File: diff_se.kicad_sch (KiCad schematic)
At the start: 7 parts

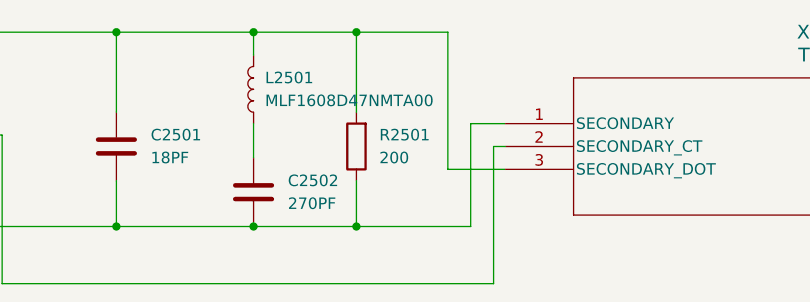
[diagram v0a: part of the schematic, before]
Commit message: Schematic Changes
Added Manufacturer/MPN/Description Fields to parts
Added libraries to project
Modified FMC schematic to use new symbol
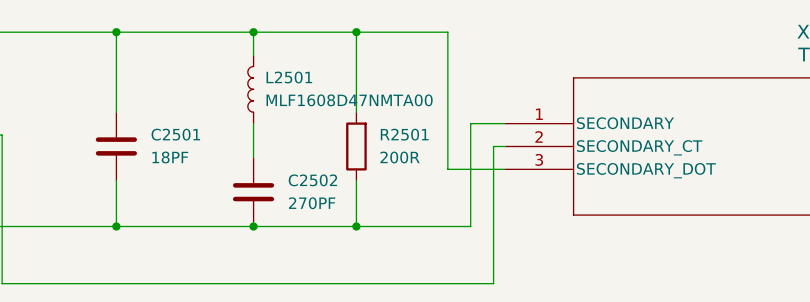
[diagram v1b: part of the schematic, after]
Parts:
- C2501: Manufacturer (none) -> Samsung; Manufacturer Part Number (none) -> CL10C180JB8NNNC
- C2502: Manufacturer (none) -> Murata; Manufacturer Part Number (none) -> GRM1885C1H271JA01D
- C2503, C2504: Manufacturer (none) -> Murata; Manufacturer Part Number (none) -> GRM1885C1H102JA01D
- L2501: Manufacturer (none) -> TDK; Manufacturer Part Number (none) -> MLF1608D47NMTA00
- R2501: value 200 -> 200R; Manufacturer (none) -> Susumu; Manufacturer Part Number (none) -> RR0816P-201-D
- XMER2501: Manufacturer (none) -> Mini-Circuits; Manufacturer Part Number (none) -> TCM4-19+
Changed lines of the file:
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@@
 			)
 		)
-		(property "Value" "200"
+		(property "Value" "200R"
 			(at 104.14 87.6299 0)
 			(effects
@@
 			)
 		)
-		(property "Description" "Resistor"
+		(property "Description" "RES SMD 200 OHM 0.5% 1/16W 0603"
 			(at 101.6 86.36 0)
 			(effects
@@
 		(property "Vendor" "digikey:RR08P200DCT-ND"
 			(at 203.2 0 0)
+			(effects
+				(font
+					(size 1.27 1.27)
+				)
+				(hide yes)
+			)
+		)
+		(property "Manufacturer" "Susumu "
+			(at 101.6 86.36 0)
+			(effects
+				(font
+					(size 1.27 1.27)
+				)
+				(hide yes)
+			)
+		)
+		(property "Manufacturer Part Number" "RR0816P-201-D "
+			(at 101.6 86.36 0)
 			(effects
 				(font
@@
 			)
 		)
-		(property "Description" "Unpolarized capacitor"
+		(property "Description" "CAP CER 1000PF 50V C0G/NP0 0603"
 			(at 204.47 88.9 0)
 			(effects
@@
 		(property "Vendor" "digikey:490-1451-1-ND"
 			(at 115.57 293.37 0)
+			(effects
+				(font
+					(size 1.27 1.27)
+				)
+				(hide yes)
+			)
+		)
+		(property "Manufacturer" "Murata"
+			(at 204.47 88.9 0)
+			(effects
+				(font
+					(size 1.27 1.27)
+				)
+				(hide yes)
+			)
+		)
+		(property "Manufacturer Part Number" "GRM1885C1H102JA01D "
+			(at 204.47 88.9 0)
 			(effects
 				(font
@@
 			)
 		)
-		(property "Description" "Inductor"
+		(property "Description" "FIXED IND 47NH 200MA 200MOHM SMD"
 			(at 90.17 80.01 0)
 			(effects
@@
 		(property "Vendor" "digikey:445-1000-1-ND"
 			(at 180.34 0 0)
+			(effects
+				(font
+					(size 1.27 1.27)
+				)
+				(hide yes)
+			)
+		)
+		(property "Manufacturer" "TDK"
+			(at 90.17 80.01 0)
+			(effects
+				(font
+					(size 1.27 1.27)
+				)
+				(hide yes)
+			)
+		)
+		(property "Manufacturer Part Number" "MLF1608D47NMTA00 "
+			(at 90.17 80.01 0)
 			(effects
 				(font
@@
 			)
 		)
-		(property "Description" "Unpolarized capacitor"
+		(property "Description" "CAP CER 1000PF 50V C0G/NP0 0603"
 			(at 204.47 83.82 0)
 			(effects
@@
 		(property "Vendor" "digikey:490-1451-1-ND"
 			(at 120.65 -120.65 0)
+			(effects
+				(font
+					(size 1.27 1.27)
+				)
+				(hide yes)
+			)
+		)
+		(property "Manufacturer" "Murata"
+			(at 204.47 83.82 0)
+			(effects
+				(font
+					(size 1.27 1.27)
+				)
+				(hide yes)
+			)
+		)
+		(property "Manufacturer Part Number" "GRM1885C1H102JA01D "
+			(at 204.47 83.82 0)
 			(effects
 				(font
@@
 			)
 		)
-		(property "Description" "Unpolarized capacitor"
+		(property "Description" "CAP CER 270PF 50V C0G/NP0 0603"
 			(at 90.17 91.44 0)
 			(effects
@@
 		(property "Vendor" "digikey:490-1437-1-ND"
 			(at 180.34 0 0)
+			(effects
+				(font
+					(size 1.27 1.27)
+				)
+				(hide yes)
+			)
+		)
+		(property "Manufacturer" "Murata"
+			(at 90.17 91.44 0)
+			(effects
+				(font
+					(size 1.27 1.27)
+				)
+				(hide yes)
+			)
+		)
+		(property "Manufacturer Part Number" "GRM1885C1H271JA01D"
+			(at 90.17 91.44 0)
 			(effects
 				(font
@@
 			)
 		)
-		(property "Description" "Unpolarized capacitor"
+		(property "Description" "CAP CER 18PF 50V C0G/NP0 0603"
 			(at 74.93 86.36 0)
 			(effects
@@
 		(property "Vendor" "digikey:1276-1089-1-ND"
 			(at 149.86 0 0)
+			(effects
+				(font
+					(size 1.27 1.27)
+				)
+				(hide yes)
+			)
+		)
+		(property "Manufacturer" "Samsung"
+			(at 74.93 86.36 0)
+			(effects
+				(font
+					(size 1.27 1.27)
+				)
+				(hide yes)
+			)
+		)
+		(property "Manufacturer Part Number" "CL10C180JB8NNNC"
+			(at 74.93 86.36 0)
 			(effects
 				(font
@@
 			)
 		)
-		(property "Description" ""
+		(property "Description" "1:4 CORE & WIRE TRANSFORMER, 10"
 			(at 118.11 83.82 0)
 			(effects
@@
 			(effects
 				(font
+					(size 1.27 1.27)
+				)
+				(hide yes)
+			)
+		)
+		(property "Manufacturer" "Mini-Circuits "
+			(at 118.11 83.82 0)
+			(effects
+				(font
+					(size 1.27 1.27)
+				)
+				(hide yes)
+			)
+		)
+		(property "Manufacturer Part Number" "TCM4-19+ "
+			(at 118.11 83.82 0)
+			(effects
+				(font

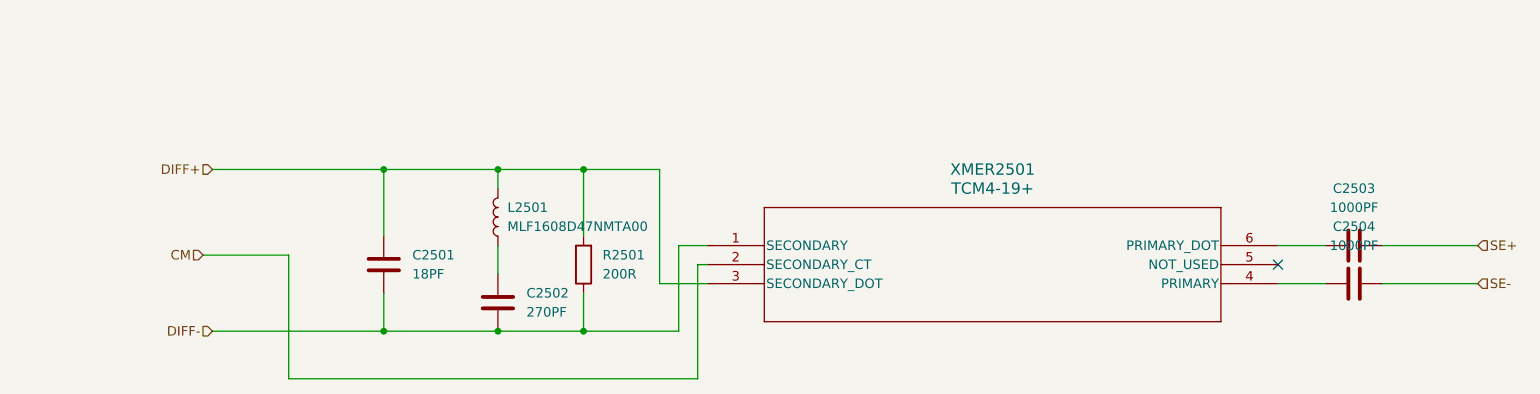
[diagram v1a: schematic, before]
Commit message: Schematics update
Cleaned up RF ADC and front end sections.
Verified that changes did not changes anything about the layout.
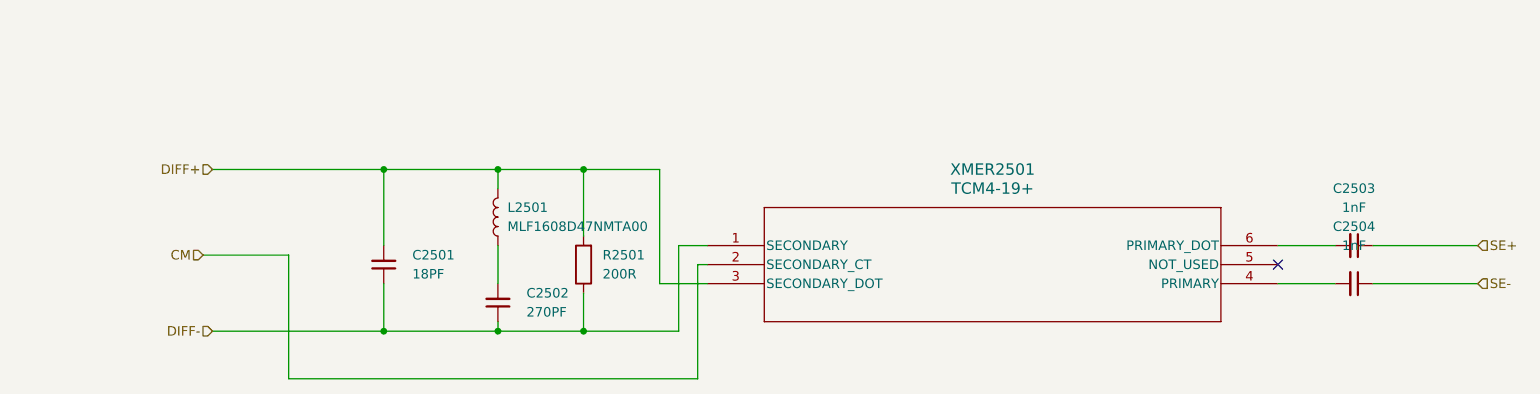
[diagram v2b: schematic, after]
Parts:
- C2501, C2502: symbol Device:C -> Device:C_Small
- C2503, C2504: value 1000PF -> 1nF; symbol Device:C -> Device:C_Small
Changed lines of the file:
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@@
 	(paper "A4")
+	(junction
+		(at 90.17 95.25)
+		(diameter 0)
+		(color 0 0 0 0)
+	)
 	(junction
 		(at 101.6 73.66)
@@
 	)
 	(junction
-		(at 90.17 95.25)
-		(diameter 0)
-		(color 0 0 0 0)
-	)
-	(junction
 		(at 74.93 95.25)
 		(diameter 0)
@@
 	(wire
 		(pts
-			(xy 74.93 73.66) (xy 74.93 82.55)
+			(xy 74.93 73.66) (xy 74.93 83.82)
 		)
 		(stroke
@@
 	(wire
 		(pts
-			(xy 74.93 90.17) (xy 74.93 95.25)
-		)
-		(stroke
-			(width 0)
-			(type default)
-		)
-	)
-	(wire
-		(pts
-			(xy 90.17 83.82) (xy 90.17 87.63)
+			(xy 74.93 88.9) (xy 74.93 95.25)
+		)
+		(stroke
+			(width 0)
+			(type default)
+		)
+	)
+	(wire
+		(pts
+			(xy 90.17 83.82) (xy 90.17 88.9)
 		)
 		(stroke
@@
 	(wire
 		(pts
-			(xy 208.28 83.82) (xy 220.98 83.82)
-		)
-		(stroke
-			(width 0)
-			(type default)
-		)
-	)
-	(wire
-		(pts
-			(xy 194.31 83.82) (xy 200.66 83.82)
+			(xy 207.01 83.82) (xy 220.98 83.82)
+		)
+		(stroke
+			(width 0)
+			(type default)
+		)
+	)
+	(wire
+		(pts
+			(xy 194.31 83.82) (xy 201.93 83.82)
+		)
+		(stroke
+			(width 0)
+			(type default)
+		)
+	)
+	(wire
+		(pts
+			(xy 90.17 93.98) (xy 90.17 95.25)
 		)
 		(stroke
@@
 	(wire
 		(pts
-			(xy 208.28 88.9) (xy 220.98 88.9)
-		)
-		(stroke
-			(width 0)
-			(type default)
-		)
-	)
-	(wire
-		(pts
-			(xy 194.31 88.9) (xy 200.66 88.9)
+			(xy 207.01 88.9) (xy 220.98 88.9)
+		)
+		(stroke
+			(width 0)
+			(type default)
+		)
+	)
+	(wire
+		(pts
+			(xy 194.31 88.9) (xy 201.93 88.9)
 		)
 		(stroke
@@
 	)
 	(symbol
-		(lib_id "Device:C")
+		(lib_id "Device:C_Small")
 		(at 204.47 88.9 270)
 		(mirror x)
@@
 			)
 		)
-		(property "Value" "1000PF"
+		(property "Value" "1nF"
 			(at 204.47 83.82 90)
 			(effects
@@
 	)
 	(symbol
-		(lib_id "Device:C")
+		(lib_id "Device:C_Small")
 		(at 204.47 83.82 270)
 		(unit 1)
@@
 			)
 		)
-		(property "Value" "1000PF"
+		(property "Value" "1nF"
 			(at 204.47 78.74 90)
 			(effects
@@
 	)
 	(symbol
-		(lib_id "Device:C")
+		(lib_id "Device:C_Small")
 		(at 90.17 91.44 180)
 		(unit 1)
@@
 	)
 	(symbol
-		(lib_id "Device:C")
+		(lib_id "Device:C_Small")
 		(at 74.93 86.36 180)
 		(unit 1)

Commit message: Updated some Schematics
- updated slowmon schematic
- updated diff to se schematic
- cleaned up DRC/ERC errors
No changes were made that effected the PCB layout
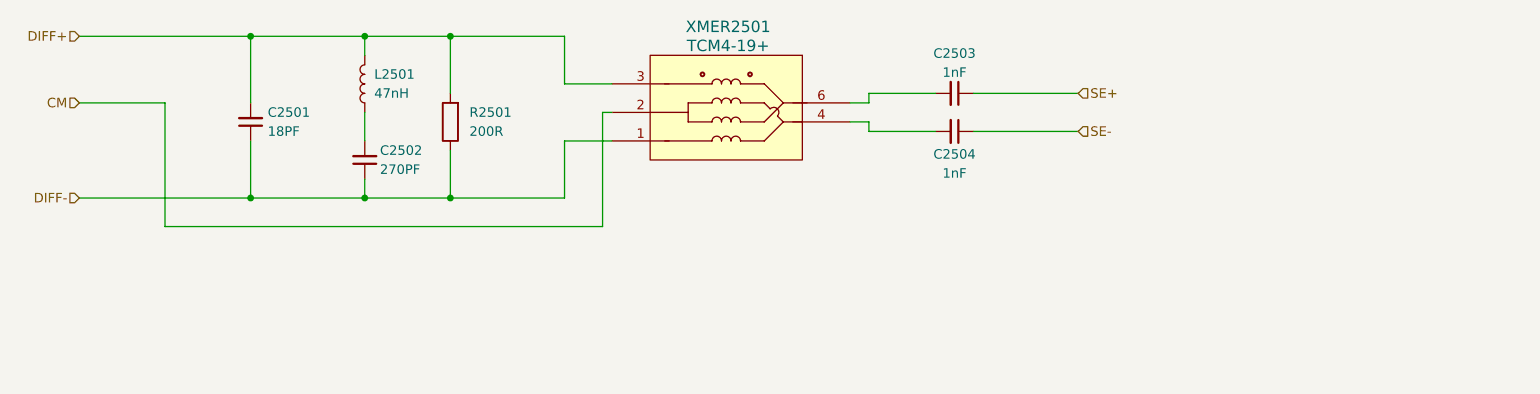
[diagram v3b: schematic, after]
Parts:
- L2501: value MLF1608D47NMTA00 -> 47nH
- XMER2501: symbol 001_symbol:TCM4-19+ -> Zest_Custom:TCM4-19+
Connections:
- no-connect marks 1 -> 0
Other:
- moved on the sheet: C2501, C2502, C2503, C2504, L2501, R2501

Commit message: Made MPEX Changes
- Minimal Changes from main branch
- Changed ADC input section TCM4-19+ to TC1-1+
- Changed DAC output section TCM4-19+ to TC4-6T+
- Changed Silkscreen text to read MPEX Zest
- Added Documentation folder with pdfs of schematics and pcb prints
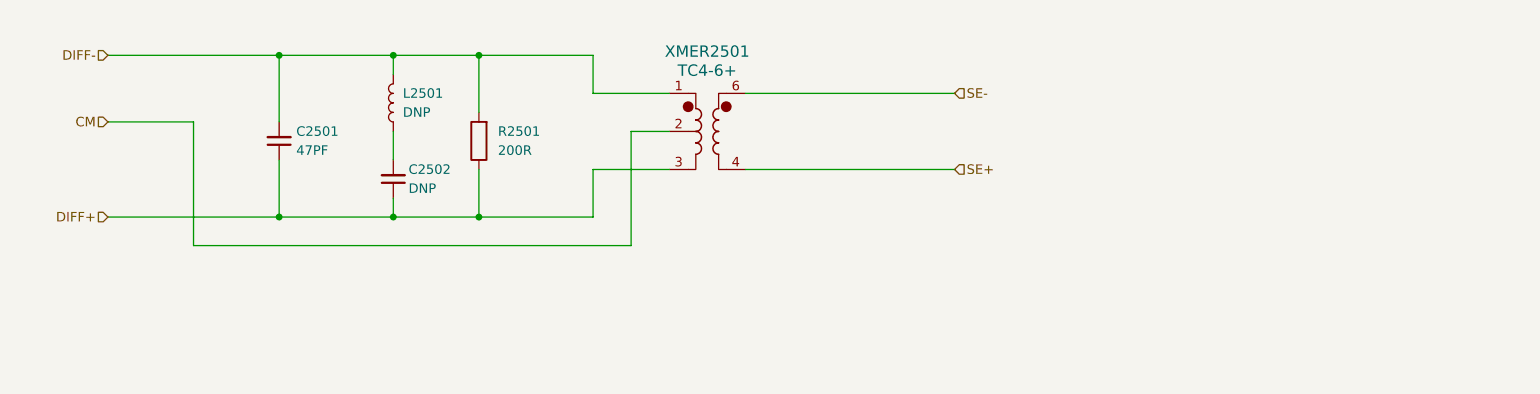
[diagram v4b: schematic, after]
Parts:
- removed C2503, C2504: 1nF, Capacitor_SMD:C_0603_1608Metric, symbol Device:C_Small
- C2501: value 18PF -> 47PF
- C2502: value 270PF -> DNP
- L2501: value 47nH -> DNP
- XMER2501: value TCM4-19+ -> TC4-6+; footprint 001_download:DB714_MNC -> Transformer_SMD:Transformer_MiniCircuits_AT224-1A; symbol Zest_Custom:TCM4-19+ -> Zest_Custom:TC4-6; Manufacturer Part Number TCM4-19+ -> TC4-6+; Vendor digikey:TCM4-19+ -> digikey:3157-TC4-6T+CT-ND
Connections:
- net DIFF+: now also C2501.1, C2502.1, R2501.1; no longer C2501.2, L2501.2, R2501.2
- net DIFF-: now also C2501.2, L2501.2, R2501.2; no longer C2501.1, C2502.1, R2501.1
- net SE+: now also XMER2501.4
- net SE-: now also XMER2501.6
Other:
- moved on the sheet: C2501, C2502, L2501, R2501

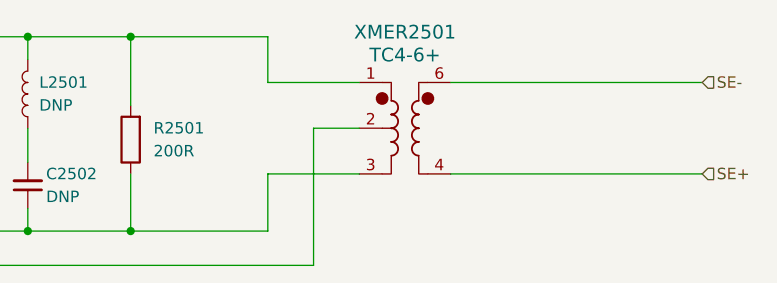
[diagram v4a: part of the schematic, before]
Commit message: Further Project cleanup
-Added BOM and fabrication files
-updated all documentation files
- Added suggested DC blocking cap at DAC outputs

-Set DRC to 5mil trace and space and fixed various violations detailed below
- Removed various small tracks overlapping IC pads on U2701,U2901,U3101,U3201
- Spaced vias 5 mil apart around U701, U201, 1201
- Moved LMK_CLKout3 pair on In4 layer away from PMOD1_1 pin
- adjusted track into pin47 on U701 to clear pin 48
- adjusted trace under U903 to give more room from ground pads/vias
- spaced out vias around pins45/46 of U201

-Many tweak to trace to go through the center of pad throughout the design
-An example is the trace around C3005
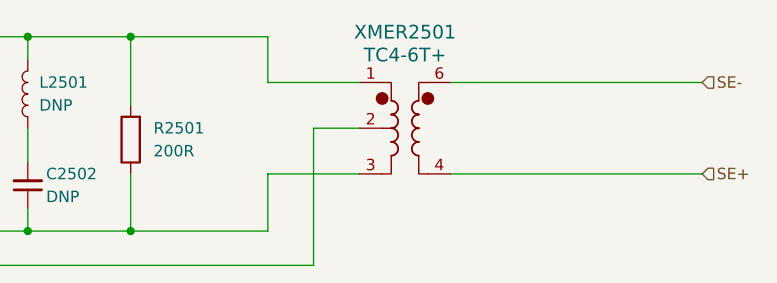
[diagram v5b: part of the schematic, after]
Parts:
- C2501: Manufacturer Samsung -> KYOCERA AVX; Manufacturer Part Number CL10C180JB8NNNC -> KGM15ACG1H470FT; Vendor digikey:1276-1089-1-ND -> digikey:478-KGM15ACG1H470FTCT-ND
- XMER2501: value TC4-6+ -> TC4-6T+
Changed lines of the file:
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@@
 			)
 		)
-		(property "Description" "CAP CER 18PF 50V C0G/NP0 0603"
+		(property "Description" "CAP CER 47PF 50V C0G/NP0 0603"
 			(at 60.96 69.85 0)
 			(effects
@@
 			)
 		)
-		(property "Vendor" "digikey:1276-1089-1-ND"
+		(property "Vendor" "digikey:478-KGM15ACG1H470FTCT-ND"
 			(at 135.89 -16.51 0)
 			(effects
@@
 			)
 		)
-		(property "Manufacturer" "Samsung"
+		(property "Manufacturer" "KYOCERA AVX"
 			(at 60.96 69.85 0)
 			(effects
@@
 			)
 		)
-		(property "Manufacturer Part Number" "CL10C180JB8NNNC"
+		(property "Manufacturer Part Number" "KGM15ACG1H470FT"
 			(at 60.96 69.85 0)
 			(effects
@@
 			)
 		)
-		(property "Value" "TC4-6+"
+		(property "Value" "TC4-6T+"
 			(at 118.11 60.452 0)
 			(effects
@@
 			)
 		)
-		(property "Datasheet" "TC4-6+"
+		(property "Datasheet" "TC4-6T+"
 			(at 123.19 60.96 0)
 			(effects

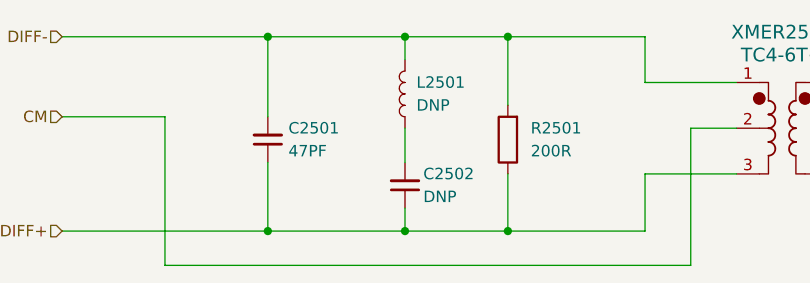
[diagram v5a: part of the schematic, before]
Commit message: Properly attributed DNP parts; Added Fabrication Notes
-Properly attributed various DNP in the project;
This includes: C210.C710,C1601,C2502,C2602,L2501,R1507,L2601,R1601,R805
- I changed the accelerometer and microphone (+it's filter)to DNP parts
  Note: both of these are obsolete parts. As part of this change I Changed R1602 (part of mic buffer) from 220k to 0R. The removal of these parts should in no way negatively effect the rest of the circuit.
-I fixed the 'value' attribute of XMER2501&XMER2601 from 'TC4-6+' -> 'TC4-6T+'
- I added some fabrication notes to the F.Fab Layer
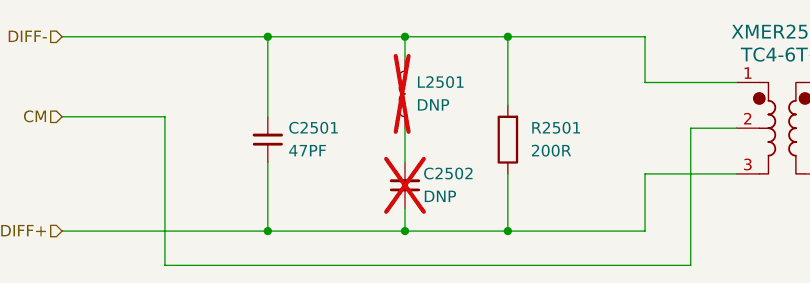
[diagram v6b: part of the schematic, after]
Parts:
- C2502, L2501: now not fitted
- XMER2501: Manufacturer Part Number TC4-6+ -> TC4-6T+
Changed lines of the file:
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@@
 		(in_bom yes)
 		(on_board yes)
-		(dnp no)
+		(dnp yes)
 		(fields_autoplaced yes)
 		(property "Reference" "L2501"
@@
 		(in_bom yes)
 		(on_board yes)
-		(dnp no)
+		(dnp yes)
 		(property "Reference" "C2502"
 			(at 78.232 73.66 0)
@@
 			)
 		)
-		(property "Manufacturer Part Number" "TC4-6+"
-			(at 123.19 60.96 0)
-			(effects
+		(property "Manufacturer Part Number" "TC4-6T+"
+			(at 123.19 60.96 0)
+			(effects
